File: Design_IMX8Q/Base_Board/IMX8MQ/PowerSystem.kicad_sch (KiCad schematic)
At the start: 1 part, among them U1 MIMX8MQ6CVAHZAB

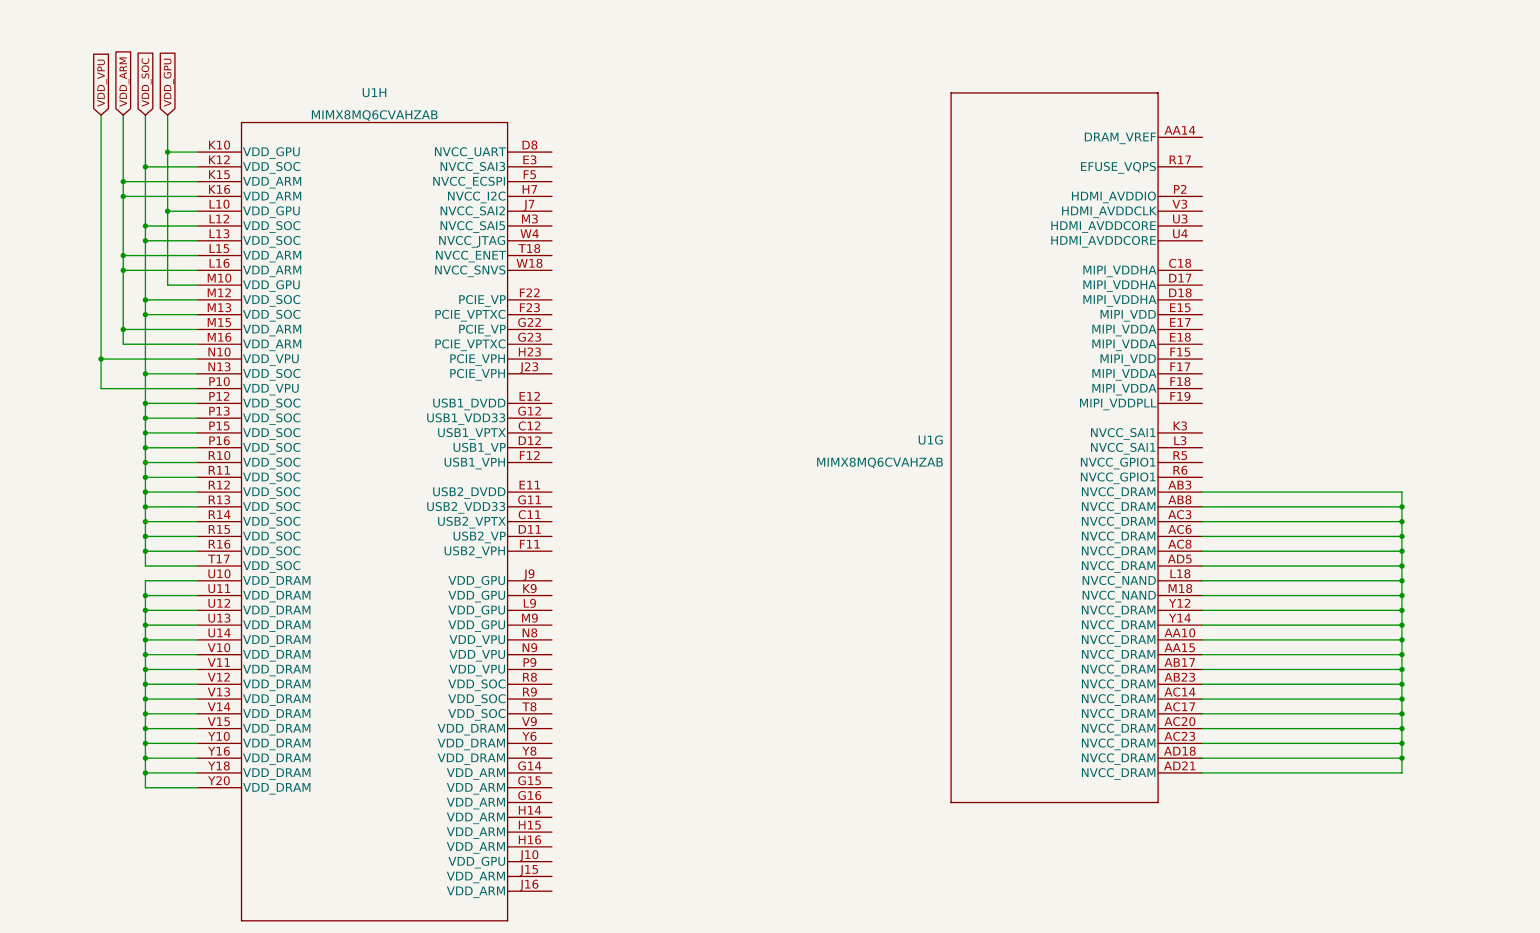
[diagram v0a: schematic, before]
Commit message: Add QSPI and more color
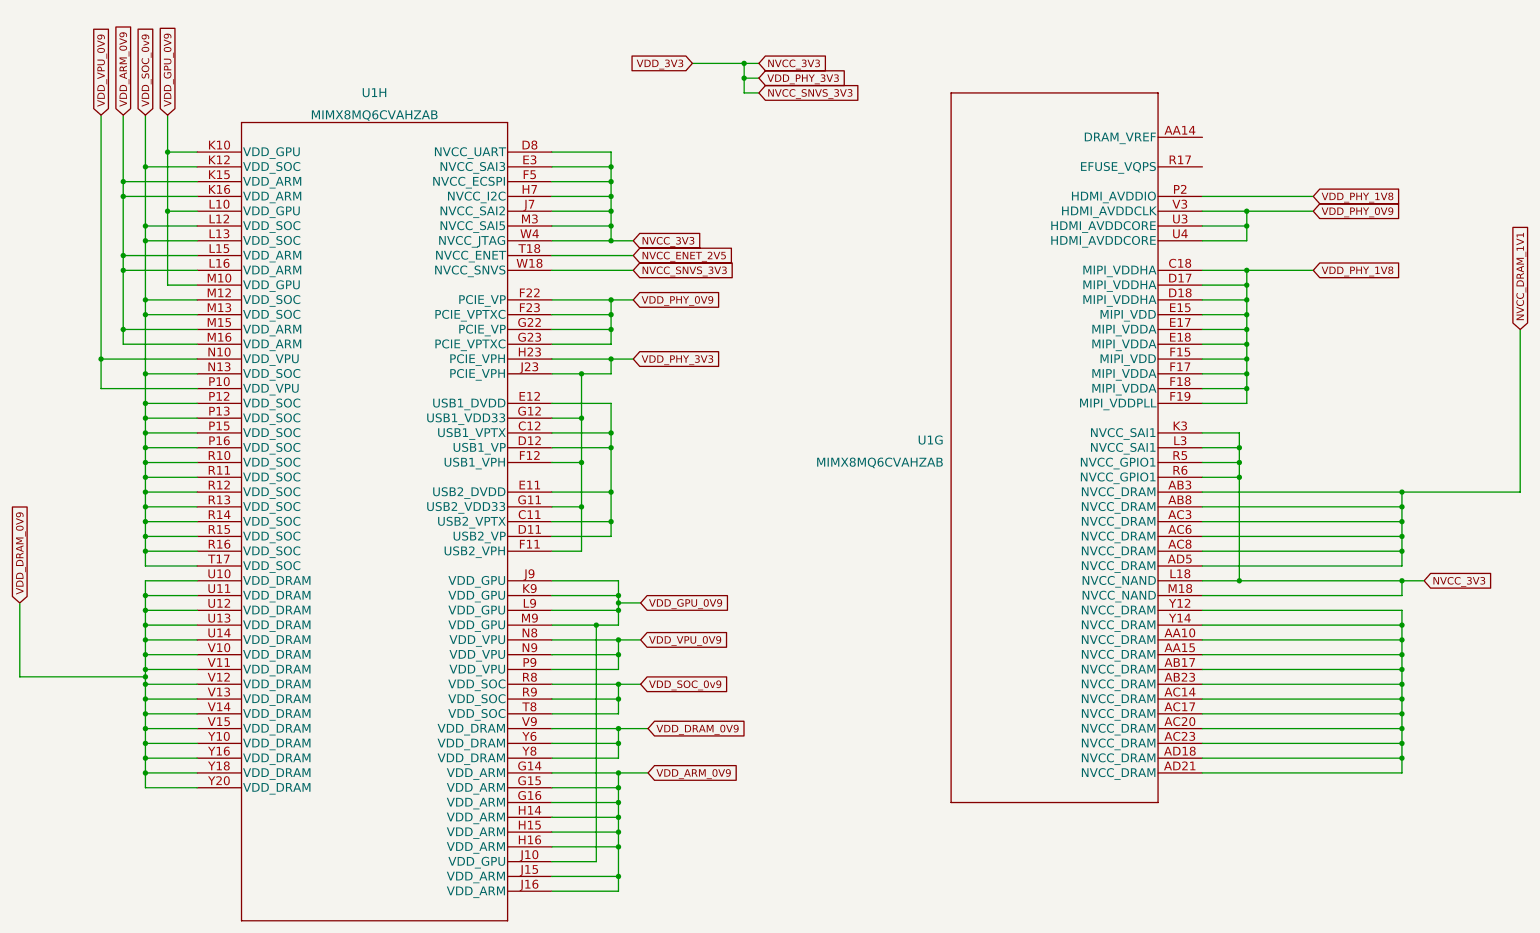
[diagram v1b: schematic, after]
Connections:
- net VDD_ARM is gone; now on net VDD_ARM_0V9: U1.K15 (VDD_ARM), U1.K16 (VDD_ARM), U1.L15 (VDD_ARM), U1.L16 (VDD_ARM), U1.M15 (VDD_ARM), U1.M16 (VDD_ARM)
- net VDD_GPU is gone; now on net VDD_GPU_0V9: U1.K10 (VDD_GPU), U1.L10 (VDD_GPU), U1.M10 (VDD_GPU)
- net VDD_SOC is gone; now on net VDD_SOC_0v9: U1.K12 (VDD_SOC), U1.L12 (VDD_SOC), U1.L13 (VDD_SOC), U1.M12 (VDD_SOC), U1.M13 (VDD_SOC), U1.N13 (VDD_SOC), U1.P12 (VDD_SOC), U1.P13 (VDD_SOC), U1.P15 (VDD_SOC), U1.P16 (VDD_SOC), U1.R10 (VDD_SOC), U1.R11 (VDD_SOC), U1.R12 (VDD_SOC), U1.R13 (VDD_SOC), U1.R14 (VDD_SOC), U1.R15 (VDD_SOC), U1.R16 (VDD_SOC), U1.T17 (VDD_SOC)
- net VDD_VPU is gone; now on net VDD_VPU_0V9: U1.N10 (VDD_VPU), U1.P10 (VDD_VPU)
- net at U1.AA10 (NVCC_DRAM), U1.AA15 (NVCC_DRAM), U1.AB17 (NVCC_DRAM)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: no longer U1.AB3 (NVCC_DRAM), U1.AB8 (NVCC_DRAM), U1.AC3 (NVCC_DRAM), U1.AC6 (NVCC_DRAM), U1.AC8 (NVCC_DRAM), U1.AD5 (NVCC_DRAM), U1.L18 (NVCC_NAND), U1.M18 (NVCC_NAND)
- net VDD_PHY_1V8: now reaches U1.C18 (MIPI_VDDHA)
- net VDD_PHY_1V8: now also U1.D17 (MIPI_VDDHA), U1.D18 (MIPI_VDDHA), U1.E15 (MIPI_VDD), U1.E17 (MIPI_VDDA), U1.E18 (MIPI_VDDA), U1.F15 (MIPI_VDD), U1.F17 (MIPI_VDDA), U1.F18 (MIPI_VDDA), U1.F19 (MIPI_VDDPLL), U1.P2 (HDMI_AVDDIO)
- net NVCC_3V3: now reaches U1.K3 (NVCC_SAI1)
- net NVCC_3V3: now also U1.D8 (NVCC_UART), U1.E3 (NVCC_SAI3), U1.F11 (USB2_VPH), U1.F12 (USB1_VPH), U1.F5 (NVCC_ECSPI), U1.G11 (USB2_VDD33), U1.G12 (USB1_VDD33), U1.H23 (PCIE_VPH), U1.H7 (NVCC_I2C), U1.J23 (PCIE_VPH), U1.J7 (NVCC_SAI2), U1.L18 (NVCC_NAND), U1.L3 (NVCC_SAI1), U1.M18 (NVCC_NAND), U1.M3 (NVCC_SAI5), U1.R5 (NVCC_GPIO1), U1.R6 (NVCC_GPIO1), U1.W18 (NVCC_SNVS), U1.W4 (NVCC_JTAG)
- net VDD_PHY_0V9: now reaches U1.U3 (HDMI_AVDDCORE)
- net VDD_PHY_0V9: now also U1.F22 (PCIE_VP), U1.F23 (PCIE_VPTXC), U1.G22 (PCIE_VP), U1.G23 (PCIE_VPTXC), U1.U4 (HDMI_AVDDCORE), U1.V3 (HDMI_AVDDCLK)
- net at U1.C11 (USB2_VPTX): now also U1.C12 (USB1_VPTX), U1.D11 (USB2_VP), U1.D12 (USB1_VP), U1.E11 (USB2_DVDD), U1.E12 (USB1_DVDD)
- net VDD_ARM_0V9: now reaches U1.G14 (VDD_ARM)
- net VDD_ARM_0V9: now also U1.G15 (VDD_ARM), U1.G16 (VDD_ARM), U1.H14 (VDD_ARM), U1.H15 (VDD_ARM), U1.H16 (VDD_ARM), U1.J15 (VDD_ARM), U1.J16 (VDD_ARM)
- net VDD_GPU_0V9: now reaches U1.J10 (VDD_GPU)
- net VDD_GPU_0V9: now also U1.J9 (VDD_GPU), U1.K9 (VDD_GPU), U1.L9 (VDD_GPU), U1.M9 (VDD_GPU)
- net VDD_VPU_0V9: now reaches U1.N8 (VDD_VPU)
- net VDD_VPU_0V9: now also U1.N9 (VDD_VPU), U1.P9 (VDD_VPU)
- net VDD_SOC_0v9: now reaches U1.R8 (VDD_SOC)
- net VDD_SOC_0v9: now also U1.R9 (VDD_SOC), U1.T8 (VDD_SOC)
- net NVCC_ENET_2V5: now reaches U1.T18 (NVCC_ENET)
- net VDD_DRAM_0V9: now reaches U1.U10 (VDD_DRAM), U1.U11 (VDD_DRAM), U1.U12 (VDD_DRAM), U1.U13 (VDD_DRAM), U1.U14 (VDD_DRAM), U1.V10 (VDD_DRAM), U1.V11 (VDD_DRAM), U1.V12 (VDD_DRAM), U1.V13 (VDD_DRAM), U1.V14 (VDD_DRAM), U1.V15 (VDD_DRAM), U1.Y10 (VDD_DRAM), U1.Y16 (VDD_DRAM), U1.Y18 (VDD_DRAM), U1.Y20 (VDD_DRAM)
- net VDD_DRAM_0V9: now also U1.V9 (VDD_DRAM), U1.Y6 (VDD_DRAM), U1.Y8 (VDD_DRAM)
- new net NVCC_DRAM_1V1: U1.AB3 (NVCC_DRAM), U1.AB8 (NVCC_DRAM), U1.AC3 (NVCC_DRAM), U1.AC6 (NVCC_DRAM), U1.AC8 (NVCC_DRAM), U1.AD5 (NVCC_DRAM)

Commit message: it was inserted power control system
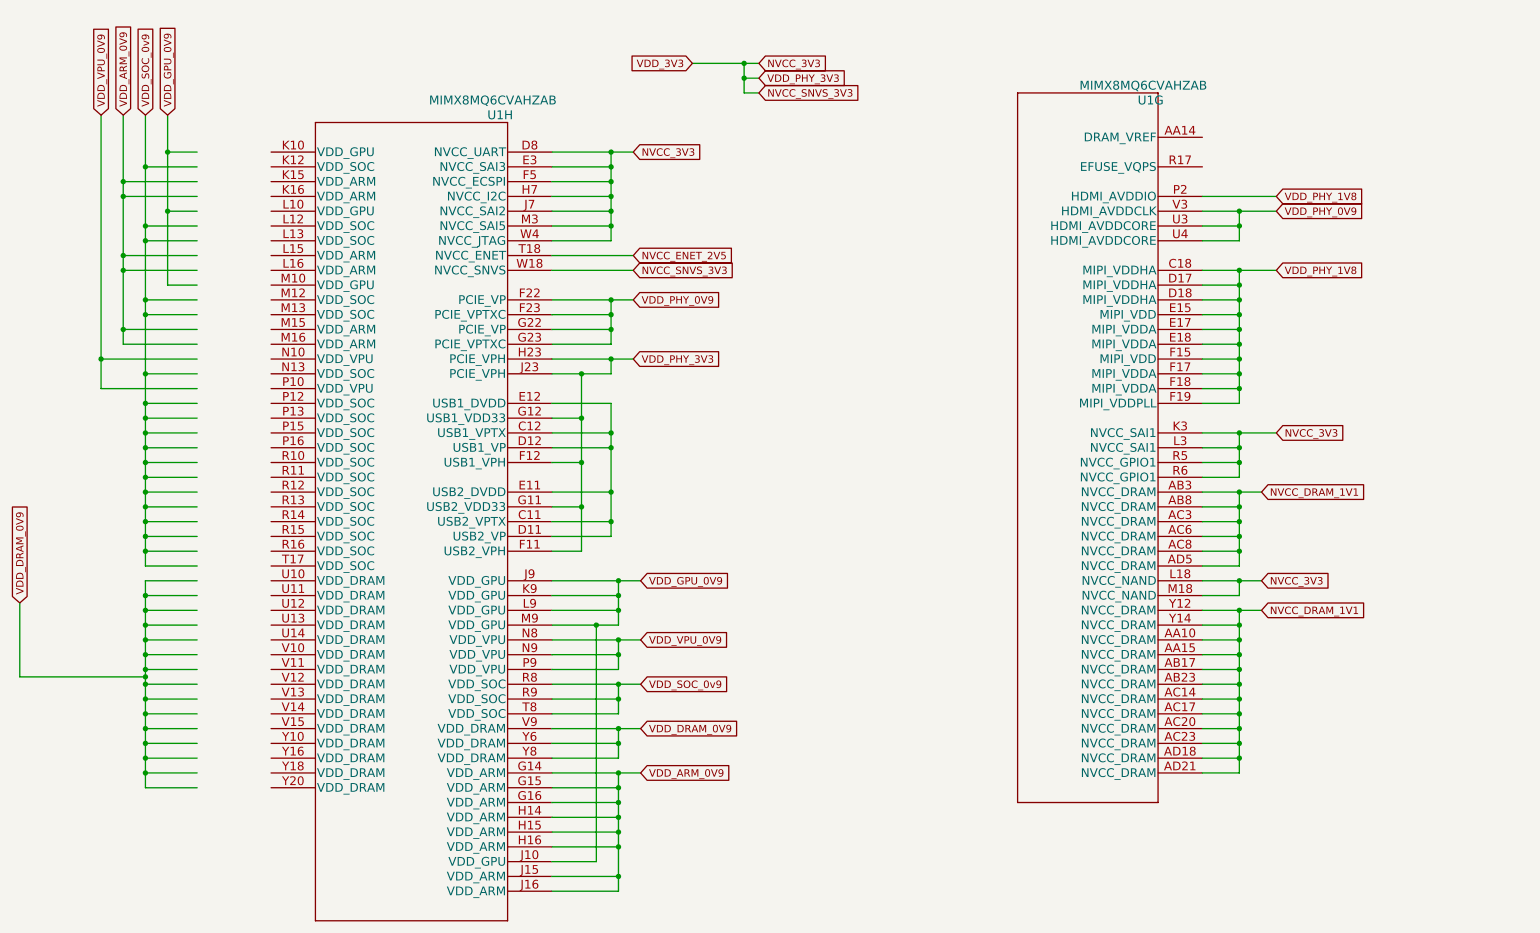
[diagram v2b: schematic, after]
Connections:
- net NVCC_DRAM_1V1: now also U1.AA10 (NVCC_DRAM), U1.AA15 (NVCC_DRAM), U1.AB17 (NVCC_DRAM), U1.AB23 (NVCC_DRAM), U1.AC14 (NVCC_DRAM), U1.AC17 (NVCC_DRAM), U1.AC20 (NVCC_DRAM), U1.AC23 (NVCC_DRAM), U1.AD18 (NVCC_DRAM), U1.AD21 (NVCC_DRAM), U1.Y12 (NVCC_DRAM), U1.Y14 (NVCC_DRAM)
- net VDD_ARM_0V9: no longer U1.K15 (VDD_ARM), U1.K16 (VDD_ARM), U1.L15 (VDD_ARM), U1.L16 (VDD_ARM), U1.M15 (VDD_ARM), U1.M16 (VDD_ARM)
- net VDD_DRAM_0V9: no longer U1.U10 (VDD_DRAM), U1.U11 (VDD_DRAM), U1.U12 (VDD_DRAM), U1.U13 (VDD_DRAM), U1.U14 (VDD_DRAM), U1.V10 (VDD_DRAM), U1.V11 (VDD_DRAM), U1.V12 (VDD_DRAM), U1.V13 (VDD_DRAM), U1.V14 (VDD_DRAM), U1.V15 (VDD_DRAM), U1.Y10 (VDD_DRAM), U1.Y16 (VDD_DRAM), U1.Y18 (VDD_DRAM), U1.Y20 (VDD_DRAM)
- net VDD_GPU_0V9: no longer U1.K10 (VDD_GPU), U1.L10 (VDD_GPU), U1.M10 (VDD_GPU)
- net VDD_SOC_0v9: no longer U1.K12 (VDD_SOC), U1.L12 (VDD_SOC), U1.L13 (VDD_SOC), U1.M12 (VDD_SOC), U1.M13 (VDD_SOC), U1.N13 (VDD_SOC), U1.P12 (VDD_SOC), U1.P13 (VDD_SOC), U1.P15 (VDD_SOC), U1.P16 (VDD_SOC), U1.R10 (VDD_SOC), U1.R11 (VDD_SOC), U1.R12 (VDD_SOC), U1.R13 (VDD_SOC), U1.R14 (VDD_SOC), U1.R15 (VDD_SOC), U1.R16 (VDD_SOC), U1.T17 (VDD_SOC)
- net VDD_VPU_0V9: no longer U1.N10 (VDD_VPU), U1.P10 (VDD_VPU)
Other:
- moved on the sheet: U1G, U1H
